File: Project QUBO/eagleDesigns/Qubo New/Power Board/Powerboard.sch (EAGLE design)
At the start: 0 parts

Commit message: 
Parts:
- added 20A_FUSE: (no value), littelfuse:BOWED-1.25"-FUSECLIPS
- added C1: 0.1u, resistor:C-USC0805
- added C2: 47n, resistor:C-USC0805
- added INPUT_CURRENT_SENSOR: ACS713SOIC, allegro:ACS713SOIC
- added INPUT_CURRENT_TO_I2C: ADC121C021, texas:ADC121C021
- added SABRE_INPUT: 2_SUPERSABRE, molex:2_SUPERSABRE
- added U$1: UWEUWE, murata:UWEUWE
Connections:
- new net 5V: C1.2, INPUT_CURRENT_SENSOR.VCC, INPUT_CURRENT_TO_I2C.ADR0, INPUT_CURRENT_TO_I2C.ADR1, INPUT_CURRENT_TO_I2C.VDD
- new net GND: C1.1, C2.1, INPUT_CURRENT_SENSOR.GND, INPUT_CURRENT_TO_I2C.GND, SABRE_INPUT.P$1
- new net N$1: 20A_FUSE.P$2, INPUT_CURRENT_SENSOR.IP+
- new net N$2: C2.2, INPUT_CURRENT_SENSOR.FILTER
- new net N$3: INPUT_CURRENT_SENSOR.VIOUT
- new net PROCESSED_INPUT: INPUT_CURRENT_SENSOR.IP-
- new net SCL: INPUT_CURRENT_TO_I2C.SCL
- new net SDA: INPUT_CURRENT_TO_I2C.SDA
- new net VBAT: 20A_FUSE.P$1, SABRE_INPUT.P$2

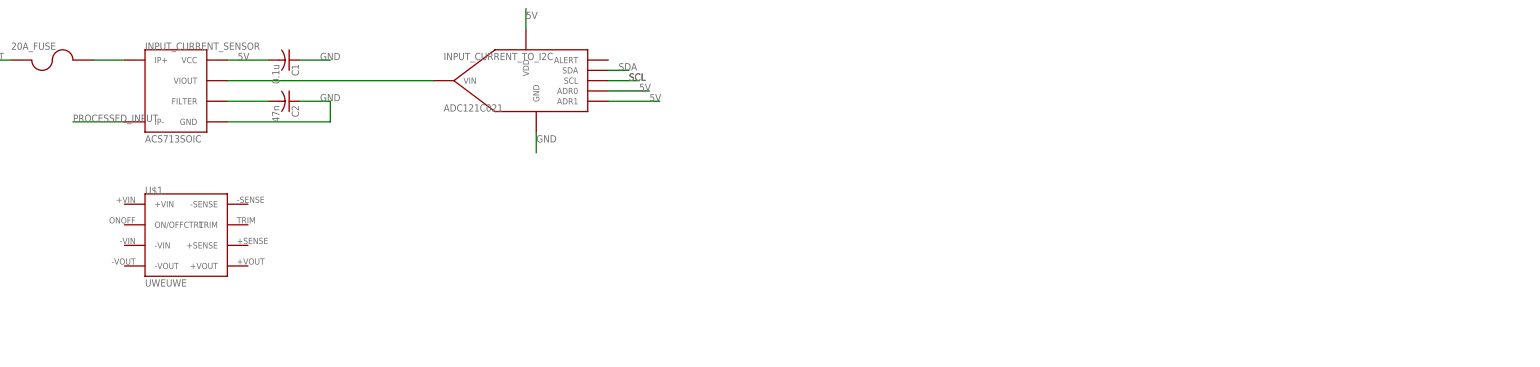
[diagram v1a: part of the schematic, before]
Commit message: 
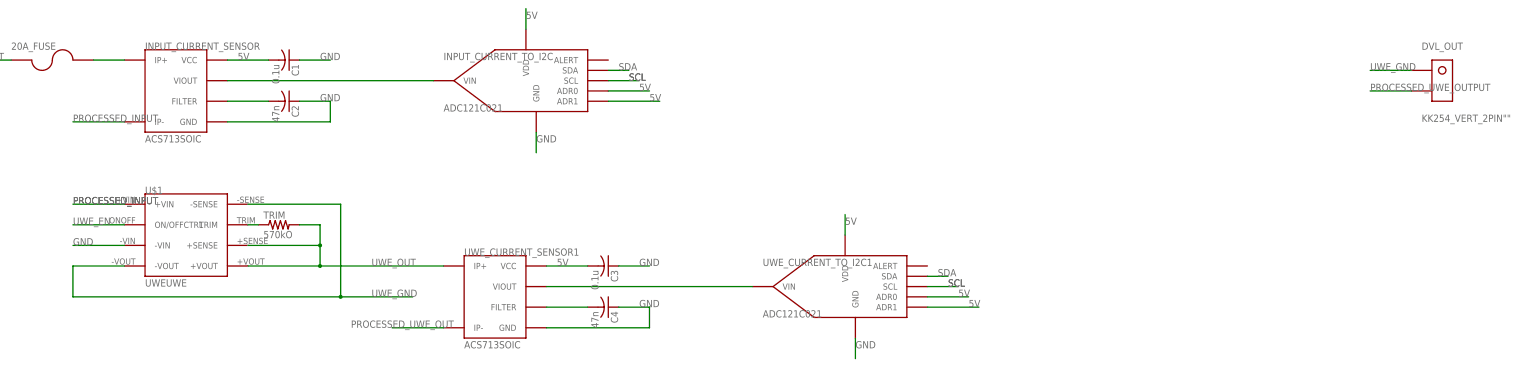
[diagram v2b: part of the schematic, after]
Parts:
- added C3: 0.1u, resistor:C-USC0805
- added C4: 47n, resistor:C-USC0805
- added DVL_OUT: KK254_VERT_2PIN"", molex:KK254_VERT_2PIN""
- added TRIM: 570kO, resistor:R-US_R0805
- added UWE_CURRENT_SENSOR1: ACS713SOIC, allegro:ACS713SOIC
- added UWE_CURRENT_TO_I2C1: ADC121C021, texas:ADC121C021
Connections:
- new net N$4: TRIM.1, U$1.TRIM
- new net N$6: C4.2, UWE_CURRENT_SENSOR1.FILTER
- new net N$7: UWE_CURRENT_SENSOR1.VIOUT
- new net PROCESSED_UWE_OUT: UWE_CURRENT_SENSOR1.IP-
- new net PROCESSED_UWE_OUTPUT: DVL_OUT.P$2
- new net UWE_EN: U$1.ON/OFFCTRL
- new net UWE_GND: DVL_OUT.P$1, U$1.-SENSE, U$1.-VOUT
- new net UWE_OUT: TRIM.2, U$1.+SENSE, U$1.+VOUT, UWE_CURRENT_SENSOR1.IP+
- net 5V: now also C3.2, UWE_CURRENT_SENSOR1.VCC, UWE_CURRENT_TO_I2C1.ADR0, UWE_CURRENT_TO_I2C1.ADR1, UWE_CURRENT_TO_I2C1.VDD
- net GND: now also C3.1, C4.1, U$1.-VIN, UWE_CURRENT_SENSOR1.GND, UWE_CURRENT_TO_I2C1.GND
- net PROCESSED_INPUT: now also U$1.+VIN
- net SCL: now also UWE_CURRENT_TO_I2C1.SCL
- net SDA: now also UWE_CURRENT_TO_I2C1.SDA
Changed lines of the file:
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@@
 <part name="INPUT_CURRENT_TO_I2C" library="texas" deviceset="ADC121C021" device=""/>
 <part name="U$1" library="murata" deviceset="UWE" device="UWE"/>
+<part name="TRIM" library="resistor" deviceset="R-US_" device="R0805" value="570kO"/>
+<part name="UWE_CURRENT_SENSOR1" library="allegro" deviceset="ACS713" device="SOIC"/>
+<part name="C3" library="resistor" deviceset="C-US" device="C0805" value="0.1u"/>
+<part name="C4" library="resistor" deviceset="C-US" device="C0805" value="47n"/>
+<part name="UWE_CURRENT_TO_I2C1" library="texas" deviceset="ADC121C021" device=""/>
+<part name="DVL_OUT" library="molex" deviceset="KK254_VERT_2PIN" device="&quot;&quot;"/>
 </parts>
 <sheets>
@@
 <instance part="INPUT_CURRENT_TO_I2C" gate="G$1" x="200.66" y="71.12"/>
 <instance part="U$1" gate="G$1" x="116.84" y="33.02"/>
+<instance part="TRIM" gate="G$1" x="139.7" y="35.56"/>
+<instance part="UWE_CURRENT_SENSOR1" gate="G$1" x="193.04" y="17.78"/>
+<instance part="C3" gate="G$1" x="220.98" y="25.4" rot="R270"/>
+<instance part="C4" gate="G$1" x="220.98" y="15.24" rot="R270"/>
+<instance part="UWE_CURRENT_TO_I2C1" gate="G$1" x="279.4" y="20.32"/>
+<instance part="DVL_OUT" gate="U1" x="426.72" y="71.12"/>
 </instances>
 <busses>
@@
 <label x="203.2" y="55.88" size="1.778" layer="95"/>
 </segment>
+<segment>
+<pinref part="U$1" gate="G$1" pin="-VIN"/>
+<wire x1="101.6" y1="30.48" x2="88.9" y2="30.48" width="0.1524" layer="91"/>
+<label x="88.9" y="30.48" size="1.778" layer="95"/>
+</segment>
+<segment>
+<pinref part="C3" gate="G$1" pin="1"/>
+<wire x1="223.52" y1="25.4" x2="231.14" y2="25.4" width="0.1524" layer="91"/>
+<label x="228.6" y="25.4" size="1.778" layer="95"/>
+</segment>
+<segment>
+<pinref part="C4" gate="G$1" pin="1"/>
+<wire x1="223.52" y1="15.24" x2="231.14" y2="15.24" width="0.1524" layer="91"/>
+<wire x1="231.14" y1="15.24" x2="231.14" y2="10.16" width="0.1524" layer="91"/>
+<pinref part="UWE_CURRENT_SENSOR1" gate="G$1" pin="GND"/>
+<wire x1="231.14" y1="10.16" x2="205.74" y2="10.16" width="0.1524" layer="91"/>
+<label x="228.6" y="15.24" size="1.778" layer="95"/>
+</segment>
+<segment>
+<pinref part="UWE_CURRENT_TO_I2C1" gate="G$1" pin="GND"/>
+<wire x1="281.94" y1="7.62" x2="281.94" y2="2.54" width="0.1524" layer="91"/>
+<label x="281.94" y="5.08" size="1.778" layer="95"/>
+</segment>
 </net>
 <net name="N$1" class="0">
@@
 <label x="231.14" y="66.04" size="1.778" layer="95"/>
 </segment>
+<segment>
+<pinref part="UWE_CURRENT_SENSOR1" gate="G$1" pin="VCC"/>
+<pinref part="C3" gate="G$1" pin="2"/>
+<wire x1="205.74" y1="25.4" x2="215.9" y2="25.4" width="0.1524" layer="91"/>
+<label x="208.28" y="25.4" size="1.778" layer="95"/>
+</segment>
+<segment>
+<pinref part="UWE_CURRENT_TO_I2C1" gate="G$1" pin="VDD"/>
+<wire x1="279.4" y1="33.02" x2="279.4" y2="38.1" width="0.1524" layer="91"/>
+<label x="279.4" y="35.56" size="1.778" layer="95"/>
+</segment>
+<segment>
+<pinref part="UWE_CURRENT_TO_I2C1" gate="G$1" pin="ADR0"/>
+<wire x1="299.72" y1="17.78" x2="309.88" y2="17.78" width="0.1524" layer="91"/>
+<label x="307.34" y="17.78" size="1.778" layer="95"/>
+</segment>
+<segment>
+<pinref part="UWE_CURRENT_TO_I2C1" gate="G$1" pin="ADR1"/>
+<wire x1="299.72" y1="15.24" x2="312.42" y2="15.24" width="0.1524" layer="91"/>
+<label x="309.88" y="15.24" size="1.778" layer="95"/>
+</segment>
 </net>
 <net name="N$2" class="0">
@@
 <wire x1="220.98" y1="73.66" x2="226.06" y2="73.66" width="0.1524" layer="91"/>
 <label x="223.52" y="73.66" size="1.778" layer="95"/>
+</segment>
+<segment>
+<pinref part="UWE_CURRENT_TO_I2C1" gate="G$1" pin="SDA"/>
+<wire x1="299.72" y1="22.86" x2="304.8" y2="22.86" width="0.1524" layer="91"/>
+<label x="302.26" y="22.86" size="1.778" layer="95"/>
 </segment>
 </net>
@@
 <label x="226.06" y="71.12" size="1.778" layer="95"/>
 </segment>
+<segment>
+<pinref part="UWE_CURRENT_TO_I2C1" gate="G$1" pin="SCL"/>
+<wire x1="299.72" y1="20.32" x2="307.34" y2="20.32" width="0.1524" layer="91"/>
+<label x="304.8" y="20.32" size="1.778" layer="95"/>
+<label x="304.8" y="20.32" size="1.778" layer="95"/>
+</segment>
 </net>
 <net name="PROCESSED_INPUT" class="0">
@@
 <label x="88.9" y="60.96" size="1.778" layer="95"/>
 </segment>
-</net>
+<segment>
+<pinref part="U$1" gate="G$1" pin="+VIN"/>
+<wire x1="101.6" y1="40.64" x2="88.9" y2="40.64" width="0.1524" layer="91"/>
+<label x="88.9" y="40.64" size="1.778" layer="95"/>
+<label x="88.9" y="40.64" size="1.778" layer="95"/>
+</segment>
+</net>
+<net name="UWE_EN" class="0">
+<segment>
+<pinref part="U$1" gate="G$1" pin="ON/OFFCTRL"/>
+<wire x1="101.6" y1="35.56" x2="88.9" y2="35.56" width="0.1524" layer="91"/>
+<label x="88.9" y="35.56" size="1.778" layer="95"/>
+</segment>
+</net>
+<net name="UWE_OUT" class="0">
+<segment>
+<pinref part="U$1" gate="G$1" pin="+VOUT"/>
+<wire x1="132.08" y1="25.4" x2="149.86" y2="25.4" width="0.1524" layer="91"/>
+<pinref part="U$1" gate="G$1" pin="+SENSE"/>
+<wire x1="149.86" y1="25.4" x2="180.34" y2="25.4" width="0.1524" layer="91"/>
+<wire x1="132.08" y1="30.48" x2="149.86" y2="30.48" width="0.1524" layer="91"/>
+<wire x1="149.86" y1="30.48" x2="149.86" y2="35.56" width="0.1524" layer="91"/>
+<pinref part="TRIM" gate="G$1" pin="2"/>
+<wire x1="149.86" y1="35.56" x2="144.78" y2="35.56" width="0.1524" layer="91"/>
+<wire x1="149.86" y1="30.48" x2="149.86" y2="25.4" width="0.1524" layer="91"/>
+<junction x="149.86" y="30.48"/>
+<junction x="149.86" y="25.4"/>
+<label x="162.56" y="25.4" size="1.778" layer="95"/>
+<pinref part="UWE_CURRENT_SENSOR1" gate="G$1" pin="IP+"/>
+</segment>
+</net>
+<net name="N$4" class="0">
+<segment>
+<pinref part="U$1" gate="G$1" pin="TRIM"/>
+<pinref part="TRIM" gate="G$1" pin="1"/>
+<wire x1="132.08" y1="35.56" x2="134.62" y2="35.56" width="0.1524" layer="91"/>
+</segment>
+</net>
+<net name="UWE_GND" class="0">
+<segment>
+<pinref part="U$1" gate="G$1" pin="-VOUT"/>
+<wire x1="101.6" y1="25.4" x2="88.9" y2="25.4" width="0.1524" layer="91"/>
+<wire x1="88.9" y1="25.4" x2="88.9" y2="17.78" width="0.1524" layer="91"/>
+<wire x1="88.9" y1="17.78" x2="154.94" y2="17.78" width="0.1524" layer="91"/>
+<pinref part="U$1" gate="G$1" pin="-SENSE"/>
+<wire x1="154.94" y1="17.78" x2="172.72" y2="17.78" width="0.1524" layer="91"/>
+<wire x1="132.08" y1="40.64" x2="154.94" y2="40.64" width="0.1524" layer="91"/>
+<wire x1="154.94" y1="40.64" x2="154.94" y2="17.78" width="0.1524" layer="91"/>
+<junction x="154.94" y="17.78"/>
+<label x="162.56" y="17.78" size="1.778" layer="95"/>
+</segment>
+<segment>
+<pinref part="DVL_OUT" gate="U1" pin="P$1"/>
+<wire x1="419.1" y1="73.66" x2="408.94" y2="73.66" width="0.1524" layer="91"/>
+<label x="408.94" y="73.66" size="1.778" layer="95"/>
+</segment>
+</net>
+<net name="N$6" class="0">
+<segment>
+<pinref part="UWE_CURRENT_SENSOR1" gate="G$1" pin="FILTER"/>
+<pinref part="C4" gate="G$1" pin="2"/>
+<wire x1="205.74" y1="15.24" x2="215.9" y2="15.24" width="0.1524" layer="91"/>
+</segment>
+</net>
+<net name="N$7" class="0">
+<segment>
+<pinref part="UWE_CURRENT_SENSOR1" gate="G$1" pin="VIOUT"/>
+<wire x1="205.74" y1="20.32" x2="256.54" y2="20.32" width="0.1524" layer="91"/>
+</segment>
+</net>
+<net name="PROCESSED_UWE_OUT" class="0">
+<segment>
+<pinref part="UWE_CURRENT_SENSOR1" gate="G$1" pin="IP-"/>
+<wire x1="180.34" y1="10.16" x2="167.64" y2="10.16" width="0.1524" layer="91"/>
+<label x="157.48" y="10.16" size="1.778" layer="95"/>
+</segment>
+</net>
+<net name="PROCESSED_UWE_OUTPUT" class="0">
+<segment>
+<pinref part="DVL_OUT" gate="U1" pin="P$2"/>
+<wire x1="419.1" y1="68.58" x2="408.94" y2="68.58" width="0.1524" layer="91"/>
+<label x="408.94" y="68.58" size="1.778" layer="95"/>
+</segment>
+</net>

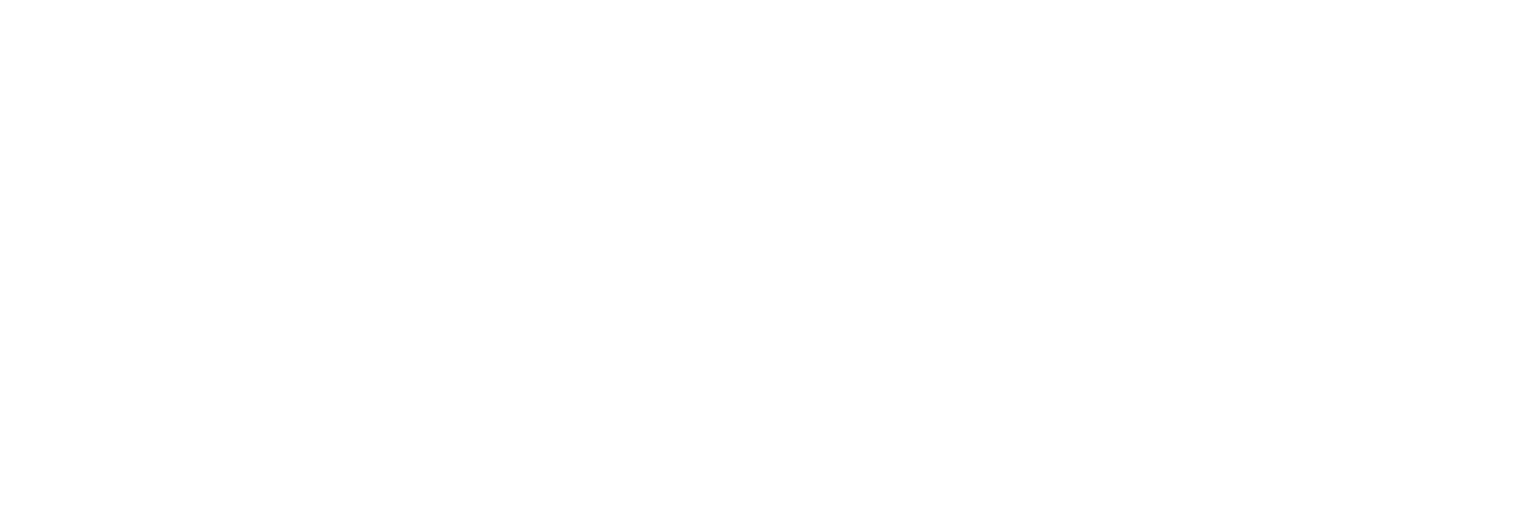
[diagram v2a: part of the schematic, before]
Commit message: 
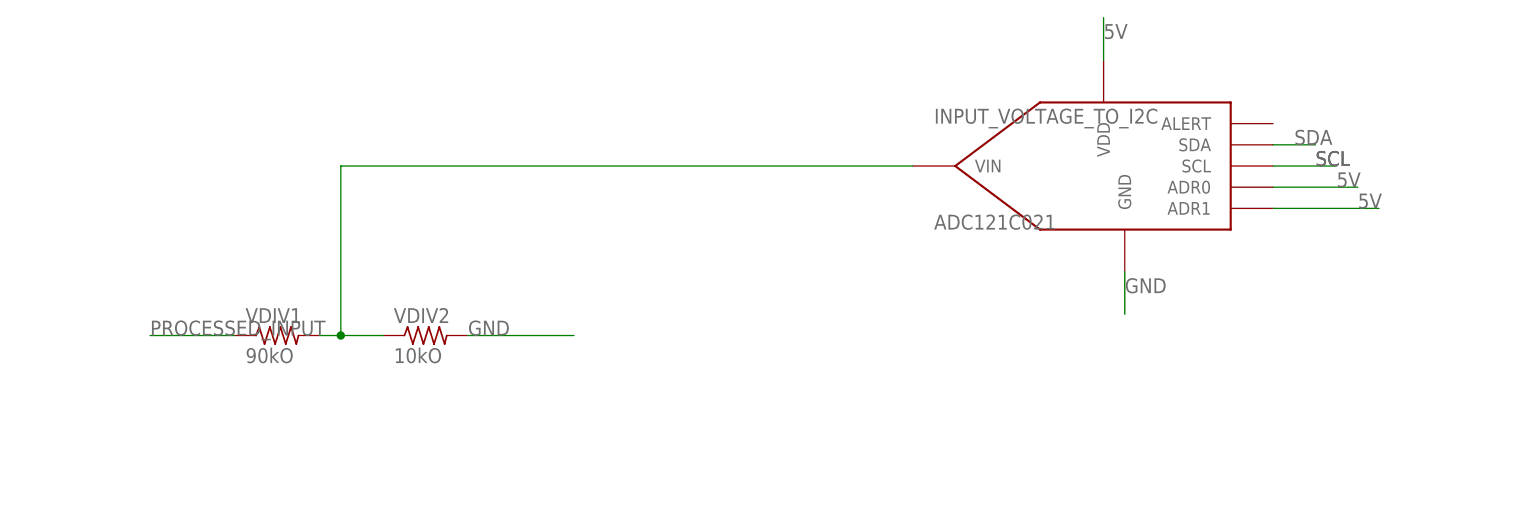
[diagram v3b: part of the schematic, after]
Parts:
- added INPUT_VOLTAGE_TO_I2C: ADC121C021, texas:ADC121C021
- added VDIV1: 90kO, resistor:R-US_R0805
- added VDIV2: 10kO, resistor:R-US_R0805
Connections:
- new net N$8: VDIV1.2, VDIV2.1
- net 5V: now also INPUT_VOLTAGE_TO_I2C.ADR0, INPUT_VOLTAGE_TO_I2C.ADR1, INPUT_VOLTAGE_TO_I2C.VDD
- net GND: now also INPUT_VOLTAGE_TO_I2C.GND, VDIV2.2
- net PROCESSED_INPUT: now also VDIV1.1
- net SCL: now also INPUT_VOLTAGE_TO_I2C.SCL
- net SDA: now also INPUT_VOLTAGE_TO_I2C.SDA
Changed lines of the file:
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@@
 <part name="UWE_CURRENT_TO_I2C1" library="texas" deviceset="ADC121C021" device=""/>
 <part name="DVL_OUT" library="molex" deviceset="KK254_VERT_2PIN" device="&quot;&quot;"/>
+<part name="VDIV1" library="resistor" deviceset="R-US_" device="R0805" value="90kO"/>
+<part name="VDIV2" library="resistor" deviceset="R-US_" device="R0805" value="10kO"/>
+<part name="INPUT_VOLTAGE_TO_I2C" library="texas" deviceset="ADC121C021" device=""/>
 </parts>
 <sheets>
@@
 <instance part="UWE_CURRENT_TO_I2C1" gate="G$1" x="279.4" y="20.32"/>
 <instance part="DVL_OUT" gate="U1" x="426.72" y="71.12"/>
+<instance part="VDIV1" gate="G$1" x="81.28" y="119.38"/>
+<instance part="VDIV2" gate="G$1" x="99.06" y="119.38"/>
+<instance part="INPUT_VOLTAGE_TO_I2C" gate="G$1" x="180.34" y="139.7"/>
 </instances>
 <busses>
@@
 <label x="281.94" y="5.08" size="1.778" layer="95"/>
 </segment>
+<segment>
+<pinref part="VDIV2" gate="G$1" pin="2"/>
+<wire x1="104.14" y1="119.38" x2="116.84" y2="119.38" width="0.1524" layer="91"/>
+<label x="104.14" y="119.38" size="1.778" layer="95"/>
+</segment>
+<segment>
+<pinref part="INPUT_VOLTAGE_TO_I2C" gate="G$1" pin="GND"/>
+<wire x1="182.88" y1="127" x2="182.88" y2="121.92" width="0.1524" layer="91"/>
+<label x="182.88" y="124.46" size="1.778" layer="95"/>
+</segment>
 </net>
 <net name="N$1" class="0">
@@
 <label x="309.88" y="15.24" size="1.778" layer="95"/>
 </segment>
+<segment>
+<pinref part="INPUT_VOLTAGE_TO_I2C" gate="G$1" pin="VDD"/>
+<wire x1="180.34" y1="152.4" x2="180.34" y2="157.48" width="0.1524" layer="91"/>
+<label x="180.34" y="154.94" size="1.778" layer="95"/>
+</segment>
+<segment>
+<pinref part="INPUT_VOLTAGE_TO_I2C" gate="G$1" pin="ADR0"/>
+<wire x1="200.66" y1="137.16" x2="210.82" y2="137.16" width="0.1524" layer="91"/>
+<label x="208.28" y="137.16" size="1.778" layer="95"/>
+</segment>
+<segment>
+<pinref part="INPUT_VOLTAGE_TO_I2C" gate="G$1" pin="ADR1"/>
+<wire x1="200.66" y1="134.62" x2="213.36" y2="134.62" width="0.1524" layer="91"/>
+<label x="210.82" y="134.62" size="1.778" layer="95"/>
+</segment>
 </net>
 <net name="N$2" class="0">
@@
 <wire x1="299.72" y1="22.86" x2="304.8" y2="22.86" width="0.1524" layer="91"/>
 <label x="302.26" y="22.86" size="1.778" layer="95"/>
+</segment>
+<segment>
+<pinref part="INPUT_VOLTAGE_TO_I2C" gate="G$1" pin="SDA"/>
+<wire x1="200.66" y1="142.24" x2="205.74" y2="142.24" width="0.1524" layer="91"/>
+<label x="203.2" y="142.24" size="1.778" layer="95"/>
 </segment>
 </net>
@@
 <label x="304.8" y="20.32" size="1.778" layer="95"/>
 </segment>
+<segment>
+<pinref part="INPUT_VOLTAGE_TO_I2C" gate="G$1" pin="SCL"/>
+<wire x1="200.66" y1="139.7" x2="208.28" y2="139.7" width="0.1524" layer="91"/>
+<label x="205.74" y="139.7" size="1.778" layer="95"/>
+<label x="205.74" y="139.7" size="1.778" layer="95"/>
+</segment>
 </net>
 <net name="PROCESSED_INPUT" class="0">
@@
 <label x="88.9" y="40.64" size="1.778" layer="95"/>
 <label x="88.9" y="40.64" size="1.778" layer="95"/>
+</segment>
+<segment>
+<pinref part="VDIV1" gate="G$1" pin="1"/>
+<wire x1="76.2" y1="119.38" x2="66.04" y2="119.38" width="0.1524" layer="91"/>
+<label x="66.04" y="119.38" size="1.778" layer="95"/>
 </segment>
 </net>
@@
 </segment>
 </net>
+<net name="N$8" class="0">
+<segment>
+<wire x1="88.9" y1="139.7" x2="157.48" y2="139.7" width="0.1524" layer="91"/>
+<pinref part="VDIV1" gate="G$1" pin="2"/>
+<pinref part="VDIV2" gate="G$1" pin="1"/>
+<wire x1="86.36" y1="119.38" x2="88.9" y2="119.38" width="0.1524" layer="91"/>
+<wire x1="88.9" y1="119.38" x2="93.98" y2="119.38" width="0.1524" layer="91"/>
+<wire x1="88.9" y1="139.7" x2="88.9" y2="119.38" width="0.1524" layer="91"/>
+<junction x="88.9" y="119.38"/>
+</segment>
+</net>

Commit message: 
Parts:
- added 10V_CURRENT_SENSOR: ACS713SOIC, allegro:ACS713SOIC
- added 10V_CURRENT_TO_I2C: ADC121C021, texas:ADC121C021
- added 10V_OUT: KK254_VERT_2PIN"", molex:KK254_VERT_2PIN""
- added 10V_REGULATOR: PTN78020, texas:PTN78020
- added ADJUST: 2.66k, resistor:R-US_R0805
- added C5: XXX, resistor:C-USC0805
- added C6: 330u, resistor:C-USC0805
- added C7: 0.1u, resistor:C-USC0805
- added C8: 47n, resistor:C-USC0805
- renumbered U$1 to UWE, UWE_CURRENT_SENSOR1 to UWE_CURRENT_SENSOR, UWE_CURRENT_TO_I2C1 to UWE_CURRENT_TO_I2C
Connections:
- new net 10V_EN: 10V_REGULATOR.!INHIBIT!
- new net 10V_OUT: 10V_CURRENT_SENSOR.IP+, 10V_REGULATOR.VO, 10V_REGULATOR.VOSENSE, C6.1
- new net N$10: 10V_CURRENT_SENSOR.FILTER, C8.2
- new net N$11: 10V_CURRENT_SENSOR.VIOUT
- new net N$5: 10V_REGULATOR.VOADJUST, ADJUST.1
- new net PROCESSED_10V_OUT: 10V_CURRENT_SENSOR.IP-, 10V_OUT.P$2
- net 5V: now also 10V_CURRENT_SENSOR.VCC, 10V_CURRENT_TO_I2C.ADR0, 10V_CURRENT_TO_I2C.ADR1, 10V_CURRENT_TO_I2C.VDD, C7.2
- net GND: now also 10V_CURRENT_SENSOR.GND, 10V_CURRENT_TO_I2C.GND, 10V_OUT.P$1, 10V_REGULATOR.GND1, 10V_REGULATOR.GND2, ADJUST.2, C5.2, C6.2, C7.1, C8.1
- net PROCESSED_INPUT: now also 10V_REGULATOR.VI, C5.1
- net SCL: now also 10V_CURRENT_TO_I2C.SCL
- net SDA: now also 10V_CURRENT_TO_I2C.SDA
